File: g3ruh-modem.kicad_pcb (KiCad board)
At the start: 2 copper layers, 160 x 100 mm, 106 parts, among them J8 CONN_01X02, P1 CONN_01X03, P2 CONN_01X06, P3 CONN_01X05, P4 C96ABC, Q1 LM7805_TO220, U1 4029, U10 LM339, U11 74HC14, U12 74HC164, U13 74HC86, U14 74HC164, U15 27C128, U16 TL084, U17 74HC74, U18 74HC164, U19 ZN429E-8, U2 27C128, U3 4029, U4 74HC164, U5 74HC74, U6 74HC86, U7 74HC164, U8 74HC161, U9 ZN429E-8

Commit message: Parts in roughly the right places and footprints verified.
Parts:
- removed J8: CONN_01X02, Pin_Headers:Pin_Header_Straight_1x02_Pitch2.54mm
- added JMP8: CONN_01X02, Pin_Headers:Pin_Header_Straight_1x02_Pitch2.54mm, F.Cu at (148.3, 102.2)
- added SPARE: DIP-16_W7.62mm, Housings_DIP:DIP-16_W7.62mm, F.Cu at (77.2, 56.5)
- added SPARE: DIP-16_W7.62mm, Housings_DIP:DIP-16_W7.62mm, F.Cu at (77.2, 81.9)
- added TP8: TEST_1P, Connectors:PINTST, F.Cu at (211.8, 112.4)
- C18, C19, C20, C21, C22: footprint Capacitors_THT:C_Axial_L3.8mm_D2.6mm_P10.00mm_Horizontal -> Capacitors_THT:C_Disc_D3.0mm_W2.0mm_P2.50mm
- C29, C30, C31, C32: footprint Capacitors_THT:C_Disc_D3.0mm_W2.0mm_P2.50mm -> Capacitors_THT:C_Axial_L3.8mm_D2.6mm_P10.00mm_Horizontal
- moved JMP5 282.9 mm to (79.7, 127.6), turned to 90 degrees
- moved TP1 269.3 mm to (87.3, 79.3)
- moved U17 266.8 mm to (77.2, 107.3)
- moved C10 255.1 mm to (94.9, 69.2)
- moved C7 253.7 mm to (115.2, 46.3)
- moved R10 250.9 mm to (102.5, 120.0)
- moved TP0 247.7 mm to (87.3, 74.3)
- moved C14 236.7 mm to (110.2, 97.1)
- moved R11 229.7 mm to (102.5, 125.1)
- moved R12 229.6 mm to (102.5, 130.2)
- moved C11 227.0 mm to (135.6, 74.3)
- moved R13 226.9 mm to (102.5, 135.2)
- moved R9 226.3 mm to (88.6, 107.3), turned to 90 degrees
- moved JMP4 224.0 mm to (107.6, 137.8), turned to 90 degrees
- moved C8 217.8 mm to (145.7, 46.3)
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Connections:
- C1 pad 2: Vref -> GND
- C10 pad 2: Vref -> GND
- C11 pad 2: Vref -> GND
- C12 pad 2: Vref -> GND
- C13 pad 2: Vref -> GND
- C14 pad 2: Vref -> GND
- C15 pad 2: Vref -> GND
- C16 pad 2: Vref -> GND
- C17 pad 2: Vref -> GND
- C2 pad 2: Vref -> GND
- C20 pad 2: Vref -> GND
- C21 pad 2: Vref -> GND
- C22 pad 2: Vref -> GND
- C23 pad 2: Vref -> GND
- C24 pad 2: Vref -> GND
- C3 pad 2: Vref -> GND
- C4 pad 2: Vref -> GND
- C5 pad 2: Vref -> GND
- C6 pad 2: Vref -> GND
- C7 pad 2: Vref -> GND
- C8 pad 2: Vref -> GND
- C9 pad 2: Vref -> GND
- JMP1 pad 3: Vref -> GND
- JMP2 pad 3: Vref -> GND
- JMP3 pad 3: Vref -> GND
- JMP4 pad 3: Vref -> GND
- JMP5 pad 3: Vref -> GND
- P1 pad 1: Vref -> GND
- P1 pad 3: Vref -> GND
- P2 pad 2: Vref -> GND
- P3 pad 2: Vref -> GND
- P3 pad 5: Vref -> GND
- Q1 pad 2: Vref -> GND
- R15 pad 1: Vref -> GND
- R8 pad 2: Vref -> GND
- TP1 pad 1: Vref -> GND
- TP3 pad 1: Vref -> GND
- TP5 pad 1: Vref -> GND
- TP7 pad 1: Vref -> GND
- U1 pad 1: Vref -> GND
- U1 pad 12: Vref -> GND
- U1 pad 13: Vref -> GND
- U1 pad 3: Vref -> GND
- U1 pad 4: Vref -> GND
- U1 pad 5: Vref -> GND
- U1 pad 8: Vref -> GND
- U10 pad 12: Vref -> GND
- U11 pad 3: Vref -> GND
- U11 pad 5: Vref -> GND
- U11 pad 7: Vref -> GND
- U12 pad 7: Vref -> GND
- U13 pad 1: Vref -> GND
- U13 pad 2: Vref -> GND
- U13 pad 7: Vref -> GND
- U14 pad 7: Vref -> GND
- U15 pad 14: Vref -> GND
- U15 pad 20: Vref -> GND
- U15 pad 22: Vref -> GND
- U16 pad 11: Vref -> GND
- U17 pad 7: Vref -> GND
- U18 pad 7: Vref -> GND
- U2 pad 14: Vref -> GND
- U2 pad 2: Vref -> GND
- U2 pad 20: Vref -> GND
- U2 pad 22: Vref -> GND
- U2 pad 26: Vref -> GND
- U3 pad 1: Vref -> GND
- U3 pad 12: Vref -> GND
- U3 pad 13: Vref -> GND
- U3 pad 3: Vref -> GND
- U3 pad 4: Vref -> GND
- U3 pad 8: Vref -> GND
- U4 pad 7: Vref -> GND
- U5 pad 7: Vref -> GND
- U6 pad 7: Vref -> GND
- U7 pad 7: Vref -> GND
- U8 pad 1: Vref -> GND
- U8 pad 10: Vref -> GND
- U8 pad 3: Vref -> GND
- U8 pad 4: Vref -> GND
- U8 pad 5: Vref -> GND
- U8 pad 6: Vref -> GND
- U8 pad 7: Vref -> GND
- U8 pad 8: Vref -> GND
- U8 pad 9: Vref -> GND
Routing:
- added copper zone on F.Cu, net GND

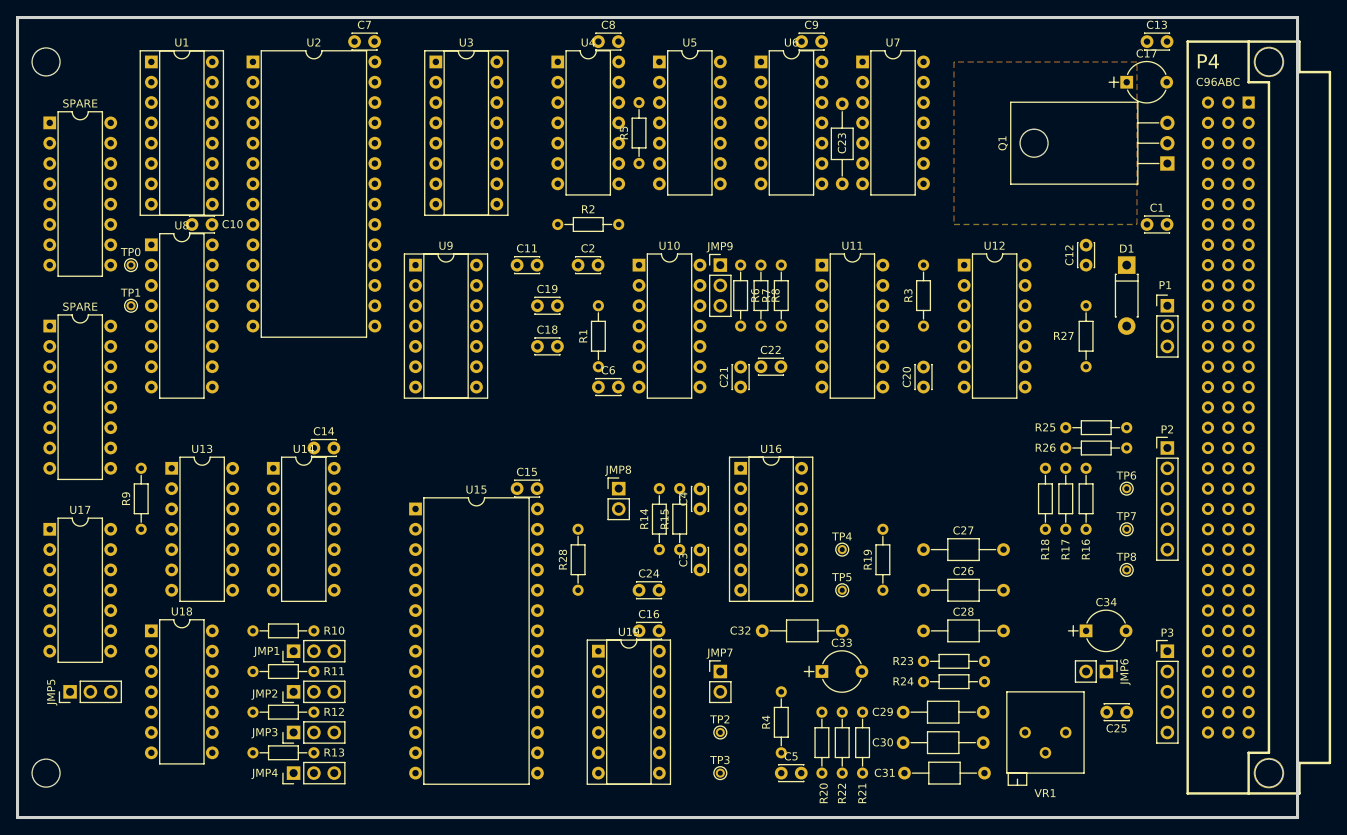
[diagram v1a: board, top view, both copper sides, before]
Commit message: Switched over to Kicad's hierachical sheets.  There are problems.
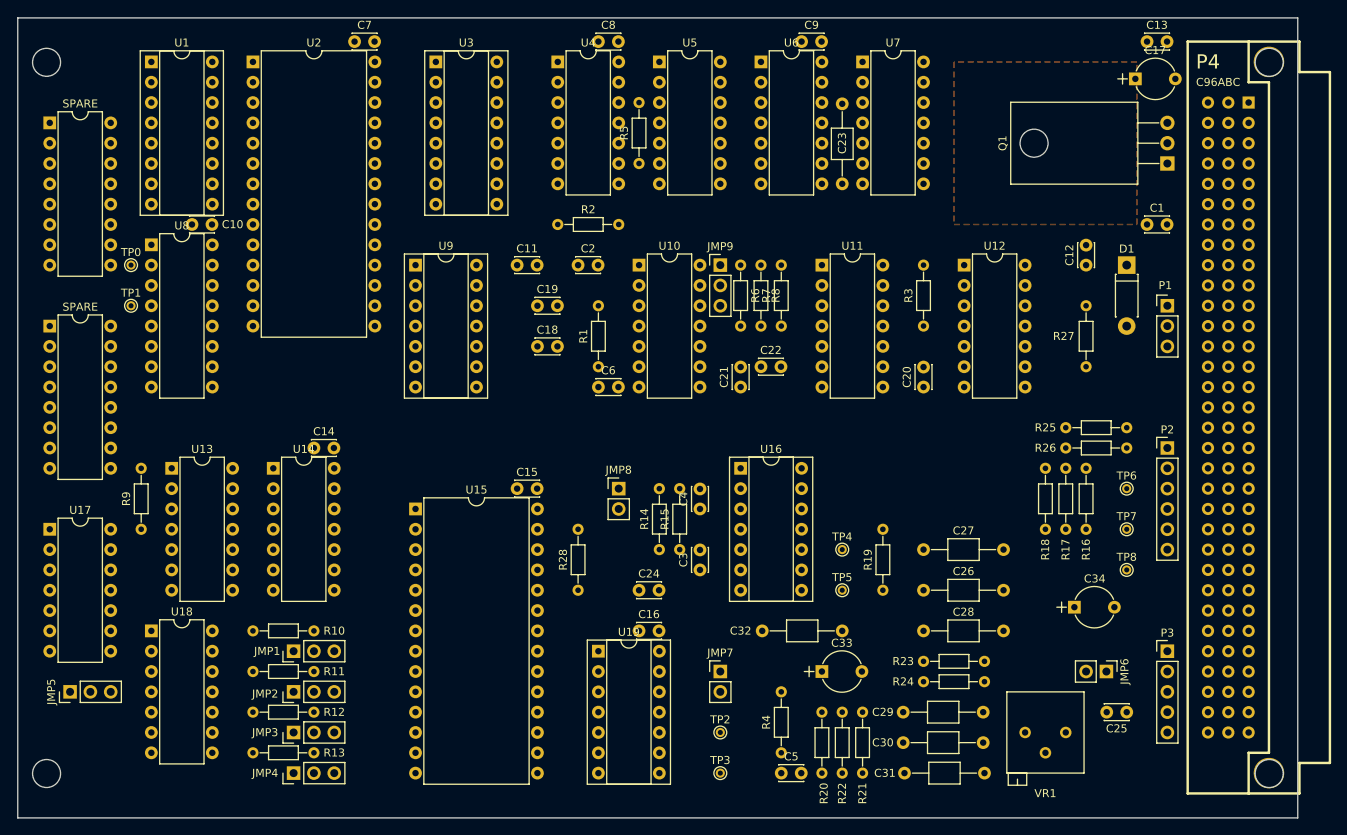
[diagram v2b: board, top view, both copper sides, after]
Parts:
- removed the REF** at (73.1, 143.3)
- added REF**: MountingHole_3.5mm, Mounting_Holes:MountingHole_3.5mm, F.Cu at (229.6, 137.8)
- added REF**: MountingHole_3.5mm, Mounting_Holes:MountingHole_3.5mm, F.Cu at (229.6, 48.9)
- added REF**: MountingHole_3.5mm, Mounting_Holes:MountingHole_3.5mm, F.Cu at (76.8, 48.9)
- added REF**: MountingHole_3.5mm, Mounting_Holes:MountingHole_3.5mm, F.Cu at (76.8, 137.8)
- moved C34 3.30 mm to (205.2, 117.0)
- moved C17 1.16 mm to (212.8, 51.0)
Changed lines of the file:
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@@
-(kicad_pcb (version 20170123) (host pcbnew "(2017-07-16 revision e797af331)-master")
+(kicad_pcb (version 4) (host pcbnew 4.0.7)
   (general
+    (links 330)
+    (no_connects 330)
+    (area 68.591429 43.294999 237.708572 143.445001)
     (thickness 1.6)
-    (drawings 0)
+    (drawings 4)
     (tracks 0)
     (zones 0)
-    (modules 109)
+    (modules 112)
     (nets 238)
   )
@@
     (pad_to_mask_clearance 0.2)
     (aux_axis_origin 0 0)
-    (grid_origin 229.55 137.77)
+    (grid_origin 73.15 43.37)
     (visible_elements FFFFF77F)
     (pcbplotparams
@@
       (hpglpenspeed 20)
       (hpglpendiameter 15)
+      (hpglpenoverlay 2)
       (psnegative false)
       (psa4output false)
@@
     (add_net Vref)
   )
+  (module Mounting_Holes:MountingHole_3.5mm (layer F.Cu)
+    (at 229.58 137.82)
+    (descr "Mounting Hole 3.5mm, no annular")
+    (tags "mounting hole 3.5mm no annular")
+    (fp_text reference REF** (at 0 -4.5) (layer F.SilkS) hide
+      (effects (font (size 1 1) (thickness 0.15)))
+    )
+    (fp_text value MountingHole_3.5mm (at 0 4.5) (layer F.Fab) hide
+      (effects (font (size 1 1) (thickness 0.15)))
+    )
+    (fp_circle (center 0 0) (end 3.75 0) (layer F.CrtYd) (width 0.05))
+    (fp_circle (center 0 0) (end 3.5 0) (layer Cmts.User) (width 0.15))
+    (pad 1 np_thru_hole circle (at 0 0) (size 3.5 3.5) (drill 3.5) (layers *.Cu *.Mask))
+  )
+  (module Mounting_Holes:MountingHole_3.5mm (layer F.Cu)
+    (at 229.58 48.92)
+    (descr "Mounting Hole 3.5mm, no annular")
+    (tags "mounting hole 3.5mm no annular")
+    (fp_text reference REF** (at 0 -4.5) (layer F.SilkS) hide
+      (effects (font (size 1 1) (thickness 0.15)))
+    )
+    (fp_text value MountingHole_3.5mm (at 0 4.5) (layer F.Fab) hide
+      (effects (font (size 1 1) (thickness 0.15)))
+    )
+    (fp_circle (center 0 0) (end 3.5 0) (layer Cmts.User) (width 0.15))
+    (fp_circle (center 0 0) (end 3.75 0) (layer F.CrtYd) (width 0.05))
+    (pad 1 np_thru_hole circle (at 0 0) (size 3.5 3.5) (drill 3.5) (layers *.Cu *.Mask))
+  )
+  (module Mounting_Holes:MountingHole_3.5mm (layer F.Cu)
+    (at 76.75 48.92)
+    (descr "Mounting Hole 3.5mm, no annular")
+    (tags "mounting hole 3.5mm no annular")
+    (fp_text reference REF** (at 0 -4.5) (layer F.SilkS) hide
+      (effects (font (size 1 1) (thickness 0.15)))
+    )
+    (fp_text value MountingHole_3.5mm (at 0 4.5) (layer F.Fab) hide
+      (effects (font (size 1 1) (thickness 0.15)))
+    )
+    (fp_circle (center 0 0) (end 3.75 0) (layer F.CrtYd) (width 0.05))
+    (fp_circle (center 0 0) (end 3.5 0) (layer Cmts.User) (width 0.15))
+    (pad 1 np_thru_hole circle (at 0 0) (size 3.5 3.5) (drill 3.5) (layers *.Cu *.Mask))
+  )
   (module Capacitors_THT:C_Disc_D3.0mm_W2.0mm_P2.50mm (layer F.Cu)
     (at 214.31 69.19)
@@
   )
   (module Capacitors_THT:CP_Radial_Tantal_D5.0mm_P5.00mm (layer F.Cu)
-    (at 211.77 51.41)
+    (at 212.85 50.99)
     (descr "CP, Radial_Tantal series, Radial, pin pitch=5.00mm, , diameter=5.0mm, Tantal Electrolytic Capacitor, http://cdn-reichelt.de/documents/datenblatt/B300/TANTAL-TB-Serie%23.pdf")
     (tags "CP Radial_Tantal series Radial pin pitch 5.00mm  diameter 5.0mm Tantal Electrolytic Capacitor")
@@
   )
   (module Capacitors_THT:CP_Radial_Tantal_D5.0mm_P5.00mm (layer F.Cu)
-    (at 206.69 119.99)
+    (at 205.23 117.03)
     (descr "CP, Radial_Tantal series, Radial, pin pitch=5.00mm, , diameter=5.0mm, Tantal Electrolytic Capacitor, http://cdn-reichelt.de/documents/datenblatt/B300/TANTAL-TB-Serie%23.pdf")
     (tags "CP Radial_Tantal series Radial pin pitch 5.00mm  diameter 5.0mm Tantal Electrolytic Capacitor")
@@
     (descr "D, DO-41_SOD81 series, Axial, Horizontal, pin pitch=7.62mm, , length*diameter=5.2*2.7mm^2, , http://www.diodes.com/_files/packages/DO-41%20(Plastic).pdf")
     (tags "D DO-41_SOD81 series Axial Horizontal pin pitch 7.62mm  length 5.2mm diameter 2.7mm")
-    (fp_text reference D1 (at -2.032 0) (layer F.SilkS)
+    (fp_text reference D1 (at -2.032 0 360) (layer F.SilkS)
       (effects (font (size 1 1) (thickness 0.15)))
     )
@@
     (fp_line (start 1.21 1.35) (end 6.41 1.35) (layer F.Fab) (width 0.1))
     (fp_line (start 1.21 -1.35) (end 1.21 1.35) (layer F.Fab) (width 0.1))
-    (fp_text user %R (at -2.032 0) (layer F.Fab)
+    (fp_text user %R (at -2.032 0 360) (layer F.Fab)
       (effects (font (size 1 1) (thickness 0.15)))
     )
@@
     (fp_line (start 1.8 4.35) (end 1.8 -1.8) (layer F.CrtYd) (width 0.05))
     (fp_line (start 1.8 -1.8) (end -1.8 -1.8) (layer F.CrtYd) (width 0.05))
-    (fp_text user %R (at 0 -2.286 90) (layer F.Fab)
+    (fp_text user %R (at 0 -2.286 450) (layer F.Fab)
       (effects (font (size 1 1) (thickness 0.15)))
     )
@@
     (descr "Resistor, Axial_DIN0204 series, Axial, Horizontal, pin pitch=7.62mm, 0.16666666666666666W = 1/6W, length*diameter=3.6*1.6mm^2, http://cdn-reichelt.de/documents/datenblatt/B400/1_4W%23YAG.pdf")
     (tags "Resistor Axial_DIN0204 series Axial Horizontal pin pitch 7.62mm 0.16666666666666666W = 1/6W length 3.6mm diameter 1.6mm")
-    (fp_text reference R27 (at 3.81 2.794) (layer F.SilkS)
+    (fp_text reference R27 (at 3.81 2.794 360) (layer F.SilkS)
       (effects (font (size 1 1) (thickness 0.15)))
     )
@@
     )
   )
-  (module EuroBoard_Outline:EuroBoard160mmX100mm_holes locked (layer F.Cu)
-    (at 73.12 143.32)
-    (descr "Outline, Eurocard, 100x160mm, with holes 3,5mm,")
-    (tags "Outline, Eurocard, 100x160mm, with holes 3,5mm,")
-    (fp_text reference REF** (at 78.74 -60.96) (layer F.SilkS) hide
-      (effects (font (size 1 1) (thickness 0.15)))
-    )
-    (fp_text value EuroBoard160mmX100mm_holes (at 85.09 -35.56) (layer F.Fab) hide
-      (effects (font (size 1 1) (thickness 0.15)))
-    )
-    (fp_line (start 160 -100) (end 0 -100) (layer Edge.Cuts) (width 0.38))
-    (fp_line (start 160 0) (end 160 -100) (layer Edge.Cuts) (width 0.38))
-    (fp_line (start 0 0) (end 160 0) (layer Edge.Cuts) (width 0.38))
-    (fp_line (start 0 -100) (end 0 0) (layer Edge.Cuts) (width 0.38))
-    (pad "" np_thru_hole circle (at 3.57 -5.55) (size 3.5 3.5) (drill 3.5) (layers *.Cu *.Mask))
-    (pad "" np_thru_hole circle (at 156.43 -5.55) (size 3.5 3.5) (drill 3.5) (layers *.Cu *.Mask))
-    (pad "" np_thru_hole circle (at 156.43 -94.45) (size 3.5 3.5) (drill 3.5) (layers *.Cu *.Mask))
-    (pad "" np_thru_hole circle (at 3.57 -94.45) (size 3.5 3.5) (drill 3.5) (layers *.Cu *.Mask))
-  )
   (module Connectors:C96ABCMC locked (layer F.Cu)
     (at 224.47 93.32 90)
@@
     )
   )
+  (module Mounting_Holes:MountingHole_3.5mm (layer F.Cu)
+    (at 76.75 137.82)
+    (descr "Mounting Hole 3.5mm, no annular")
+    (tags "mounting hole 3.5mm no annular")
+    (fp_text reference REF** (at 0 -4.5) (layer F.SilkS) hide
+      (effects (font (size 1 1) (thickness 0.15)))
+    )
+    (fp_text value MountingHole_3.5mm (at 0 4.5) (layer F.Fab) hide
+      (effects (font (size 1 1) (thickness 0.15)))
+    )
+    (fp_circle (center 0 0) (end 3.5 0) (layer Cmts.User) (width 0.15))
+    (fp_circle (center 0 0) (end 3.75 0) (layer F.CrtYd) (width 0.05))
+    (pad 1 np_thru_hole circle (at 0 0) (size 3.5 3.5) (drill 3.5) (layers *.Cu *.Mask))
+  )
+  (gr_line (start 233.15 143.37) (end 73.15 143.37) (angle 90) (layer Edge.Cuts) (width 0.15))
+  (gr_line (start 233.15 43.37) (end 233.15 143.37) (angle 90) (layer Edge.Cuts) (width 0.15))
+  (gr_line (start 73.15 43.37) (end 233.15 43.37) (angle 90) (layer Edge.Cuts) (width 0.15))
+  (gr_line (start 73.15 143.37) (end 73.15 43.37) (angle 90) (layer Edge.Cuts) (width 0.15))
   (zone (net 236) (net_name GND) (layer F.Cu) (hatch full 0.508)
     (connect_pads (clearance 0.508))
